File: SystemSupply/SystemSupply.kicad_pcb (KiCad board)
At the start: 2 copper layers, 75 x 75 mm, 52 parts, among them J1 Conn_01x01, J10 Screw_Terminal_01x02, J2 Conn_01x01, J3 4P4C, J4 Conn_01x01, J5 Conn_01x01, J6 Screw_Terminal_01x02, J7 4P4C, J8 Screw_Terminal_01x02, J9 Screw_Terminal_01x02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

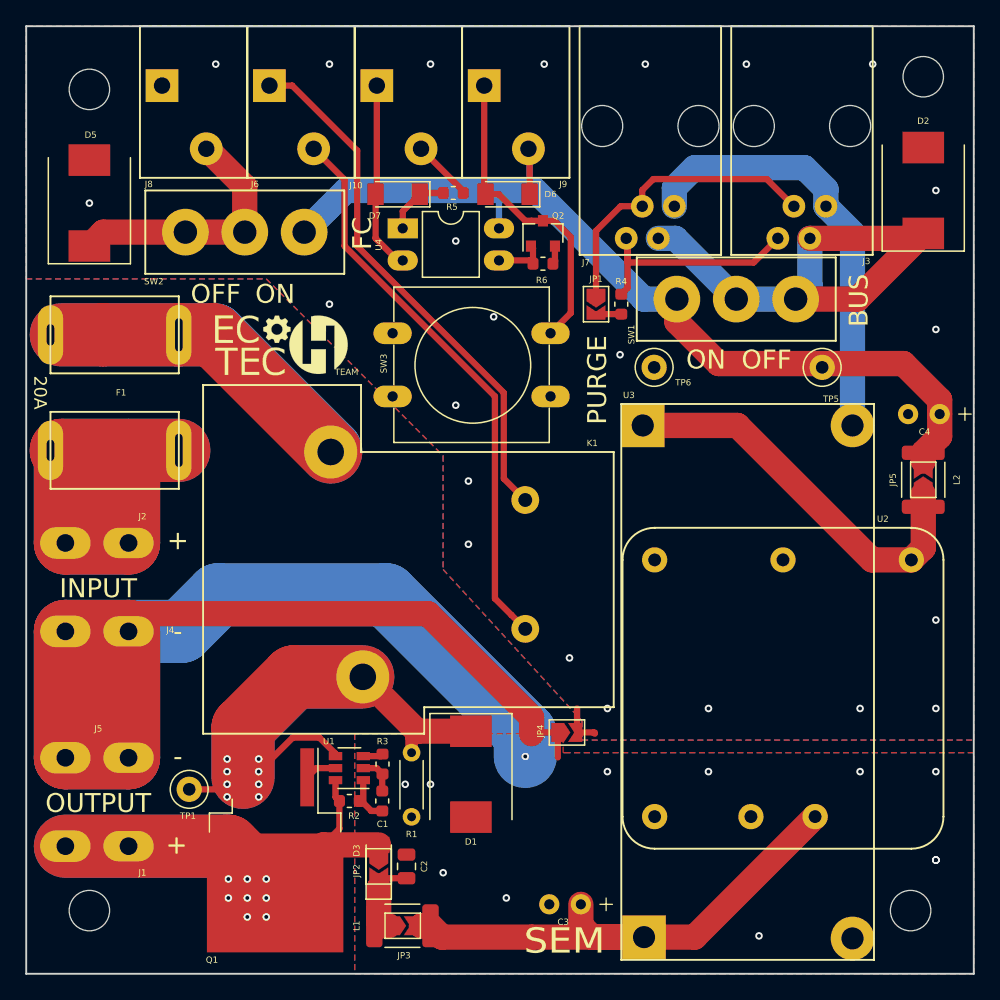
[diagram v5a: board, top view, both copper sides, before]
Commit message: Added 3D models to the library
Squashed commit of the following:

commit 8070c09fc3d8f70a7cb84d0f12b6782c2c87c14c
Author: Paweł <mackipawel@gmail.com>
Date:   Mon May 6 20:26:56 2019 +0200

    Added SystemSupply 3d models.

commit 94ef8708632c7bc91211bc6ded4e0c8fb9ccef4a
Author: Paweł <mackipawel@gmail.com>
Date:   Mon May 6 01:08:52 2019 +0200

    Added 3D models to SystemSupply.

commit eb394d70be979be958e4acab21accb1817e8e0e5
Author: Paweł <mackipawel@gmail.com>
Date:   Mon May 6 00:55:39 2019 +0200

    Added 3D model to MotorController.

commit fd89e01e0ef36f85afad3e8686d3deffdf36454d
Author: Paweł <mackipawel@gmail.com>
Date:   Mon May 6 00:40:56 2019 +0200

    Added 3D models in MotorDriver.

commit 899d106fa8d45578189a4955328047d8f9558beb
Author: Paweł <mackipawel@gmail.com>
Date:   Mon May 6 00:09:40 2019 +0200

    Added 3D models to SafetySupply.

commit 06c807994bb47431d2802a96796741a0e8fb9ae5
Author: Paweł <mackipawel@gmail.com>
Date:   Sun May 5 23:17:48 2019 +0200

    Added 3D models to SafetySystem.
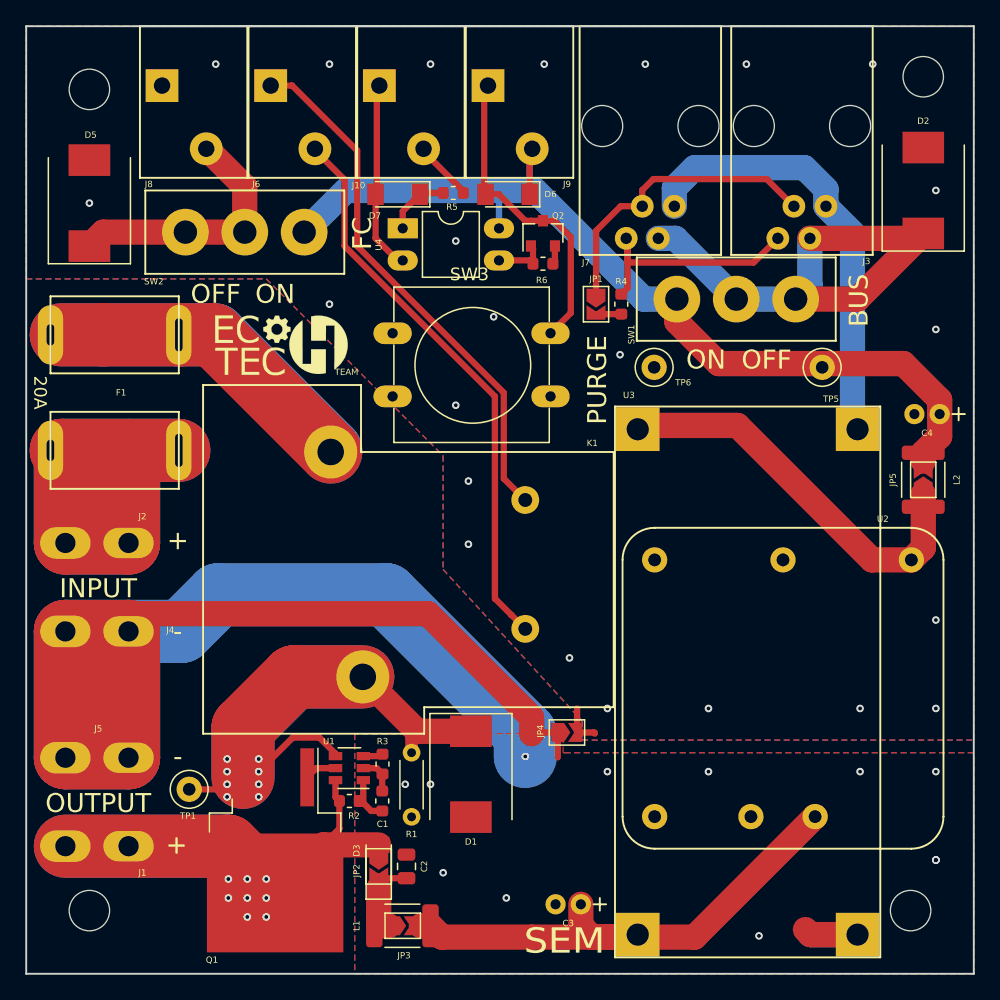
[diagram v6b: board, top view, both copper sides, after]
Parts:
- C3, C4: footprint Footprints:C_Radial_D6.3mm_H11.0mm_P2.50mm -> Footprints:C_Radial_D5.0mm_H11.0mm_P2.00mm
- SW3: footprint Button_Switch_THT:SW_PUSH-12mm -> Footprints:SW_PUSH-12mm
- moved J9 0.30 mm to (94.8, 90.0)
- moved J10 0.20 mm to (86.2, 90.0)
- moved J6 0.10 mm to (77.6, 90.0)
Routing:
- net GNDPWR: track 149.2 -> 157.4 mm

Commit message: Adding gerbers
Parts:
- moved G1 1.53 mm to (81.8, 115.0)

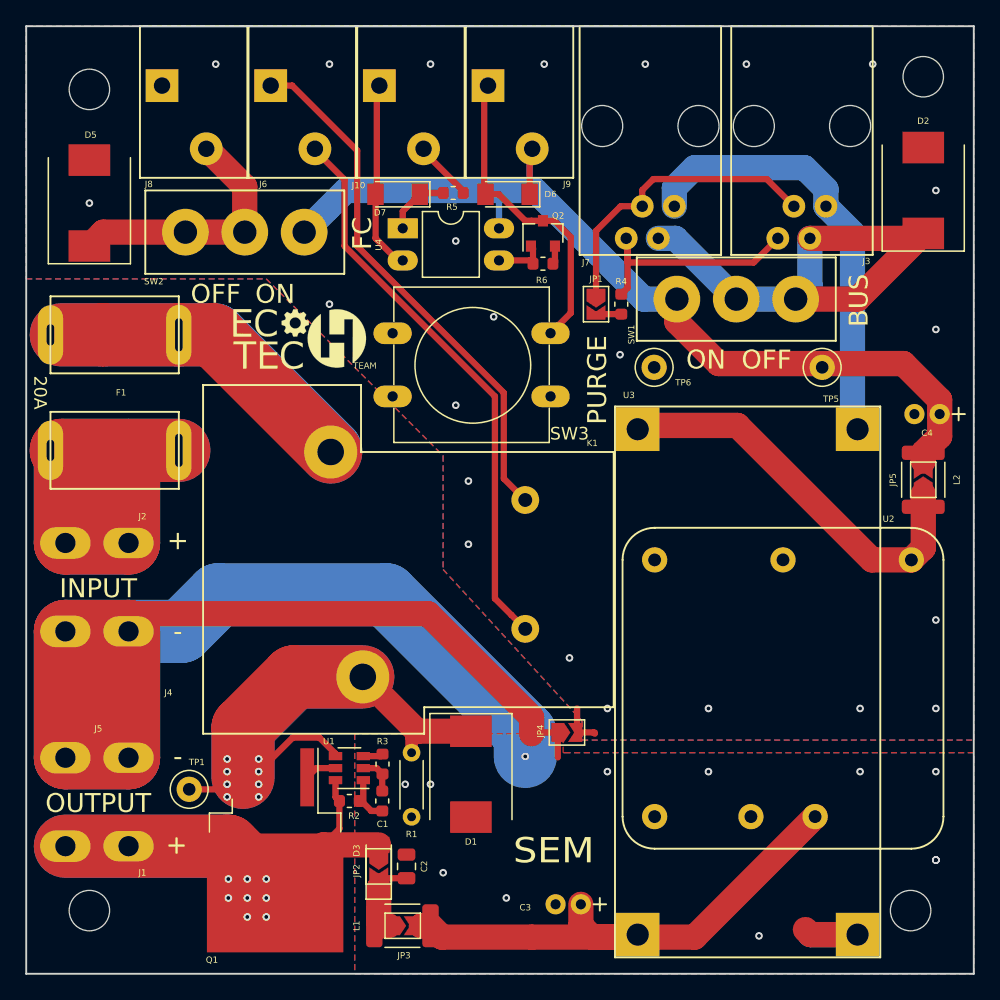
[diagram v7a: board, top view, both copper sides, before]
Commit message: Changed all via diameters to 0.7. Added project and version label on silk screen. Added more grounding vias.
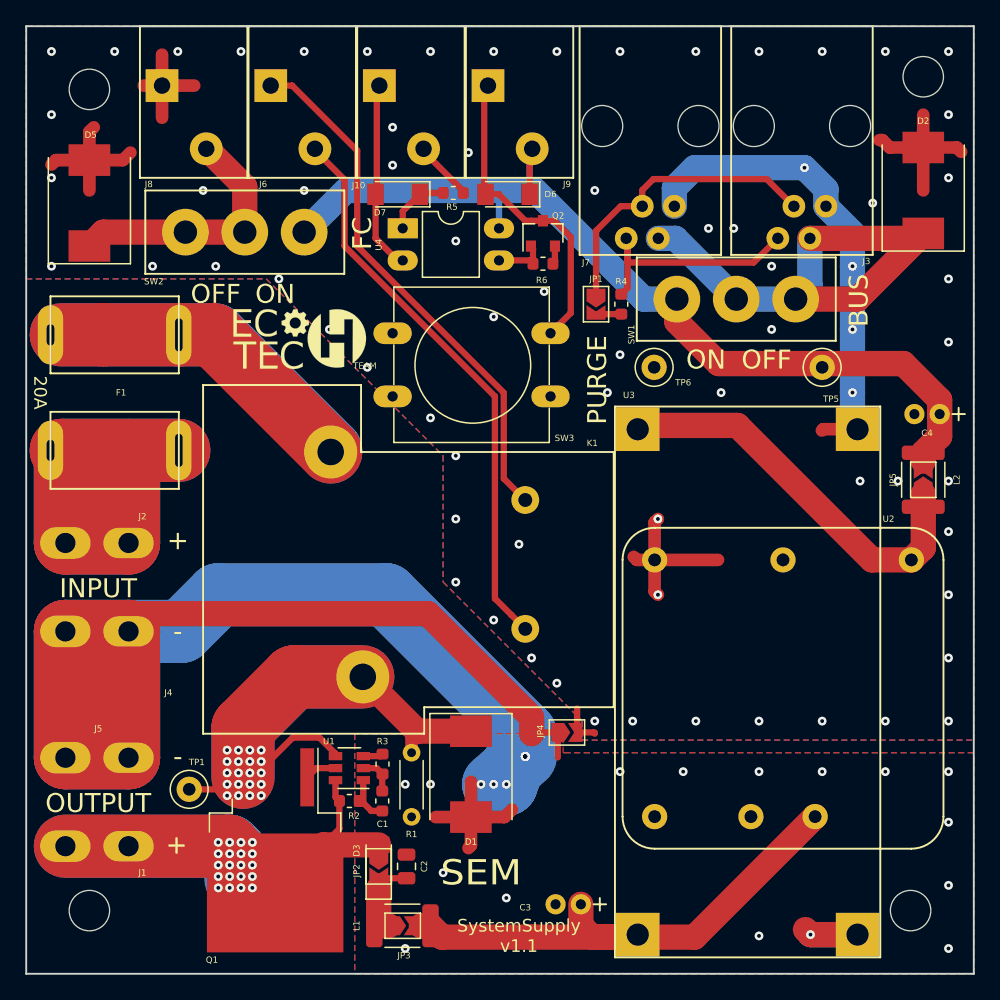
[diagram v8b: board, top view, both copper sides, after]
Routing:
- net GND: track 39.3 -> 88.8 mm, vias 23 -> 71
- net GNDPWR: track 157.4 -> 175.8 mm, vias 13 -> 24
- net +24V: track 64.2 -> 54.9 mm, vias 8 -> 20
- net Net-(D1-Pad1): vias 8 -> 20
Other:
- net class Default: via_dia 0.6 -> 0.7
- rule via_min_size: 0.4 -> 0.7
- board text added: "SystemSupply v1.1"
